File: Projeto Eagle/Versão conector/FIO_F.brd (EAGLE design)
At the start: 15.8 x 21.5 mm, 4 parts, among them J1 CONECTOR_FEMEA

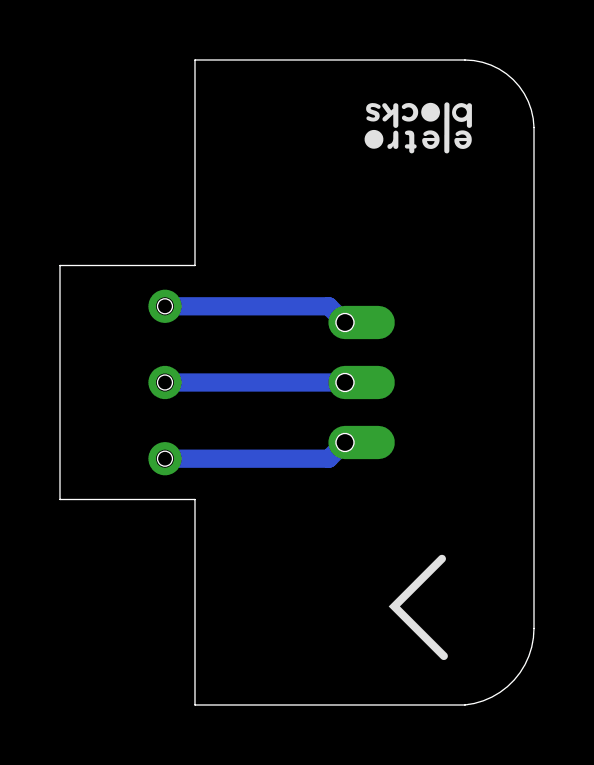
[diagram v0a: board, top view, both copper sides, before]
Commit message: correção de pads e adição de label de versionamento
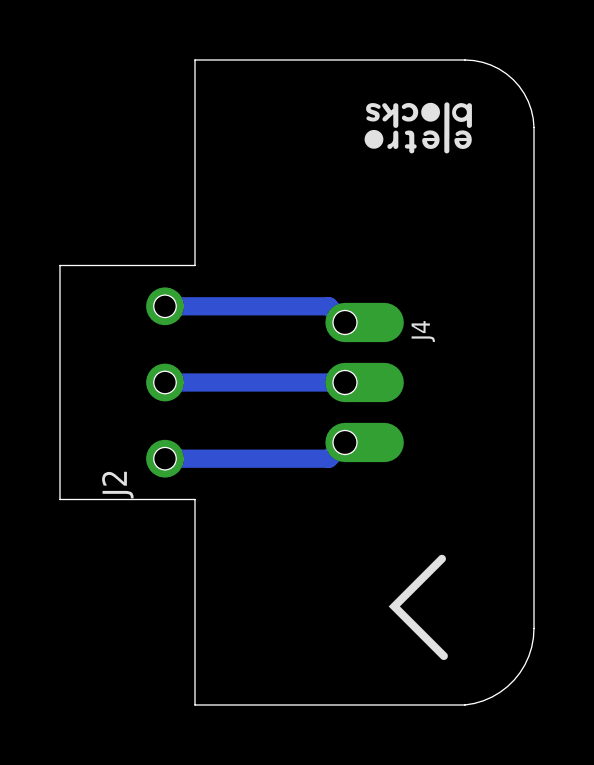
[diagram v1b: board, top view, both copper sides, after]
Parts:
- renumbered J1 to J2, U$2 to J4
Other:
- board text added: "V1.0.1"
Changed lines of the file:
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@@
 <vertex x="5.381978125" y="19.43508125"/>
 </polygon>
+<text x="-1.14" y="21.3" size="0.6096" layer="22" font="fixed" rot="MR270">V1.0.1</text>
 </plain>
 <attributes>
@@
 </groups>
 <elements>
-<element name="J1" library="Eletroblocks Lib" package="3CONECTOR" override_package3d_urn="urn:adsk.eagle:package:22394112/2" override_package_urn="urn:adsk.eagle:footprint:22394113/1" value="CONECTOR_FEMEA" x="-4.5" y="10.75" smashed="yes" grouprefs="BLOCO"/>
+<element name="J2" library="Eletroblocks Lib" package="3CONECTOR" override_package3d_urn="urn:adsk.eagle:package:22394112/2" override_package_urn="urn:adsk.eagle:footprint:22394113/1" override_locally_modified="yes" value="CONECTOR_FEMEA" x="-4.5" y="10.75" smashed="yes" grouprefs="BLOCO">
+<attribute name="NAME" x="-5.77" y="6.94" size="0.8128" layer="21" font="fixed" rot="R90"/>
+</element>
 <element name="U$1" library="Eletroblocks Lib" package="PAD" value="PAD" x="1.5" y="12.75" smashed="yes"/>
-<element name="U$2" library="Eletroblocks Lib" package="PAD" override_package3d_urn="urn:adsk.eagle:package:22394060/2" override_package_urn="urn:adsk.eagle:footprint:22394061/1" value="PAD" x="1.5" y="10.75" smashed="yes"/>
+<element name="J4" library="Eletroblocks Lib" package="PAD" override_package3d_urn="urn:adsk.eagle:package:22394060/4" override_package_urn="urn:adsk.eagle:footprint:22394061/2" value="PAD" x="1.5" y="10.75" smashed="yes">
+<attribute name="NAME" x="3.72" y="12.84" size="0.6096" layer="21" font="fixed" rot="R270"/>
+</element>
 <element name="VCC" library="Eletroblocks Lib" package="PAD" value="PAD" x="1.5" y="8.75" smashed="yes"/>
 </elements>
 <signals>
 <signal name="SIGNAL_IN">
-<contactref element="J1" pad="2"/>
-<contactref element="U$2" pad="P$1"/>
+<contactref element="J2" pad="2"/>
+<contactref element="J4" pad="P$1"/>
 <wire x1="-4.5" y1="10.75" x2="1.5" y2="10.75" width="0.6096" layer="16"/>
 </signal>
 <signal name="GND">
-<contactref element="J1" pad="1"/>
+<contactref element="J2" pad="1"/>
 <contactref element="U$1" pad="P$1"/>
 <wire x1="-4.5" y1="13.29" x2="0.96" y2="13.29" width="0.6096" layer="16"/>
@@
 </signal>
 <signal name="VCC">
-<contactref element="J1" pad="3"/>
+<contactref element="J2" pad="3"/>
 <contactref element="VCC" pad="P$1"/>
 <wire x1="-4.5" y1="8.21" x2="0.96" y2="8.21" width="0.6096" layer="16"/>
